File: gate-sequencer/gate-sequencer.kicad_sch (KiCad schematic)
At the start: 153 parts, among them J1 Gate 8, J10 Gate 6, J11 Gate 10, J12 Gate 14, J13 Gate 1, J14 Gate 5, J15 Gate 9, J16 Gate 13, J17 Clock, J18 Conn_01x34_Socket, J19 Power, J2 Gate 4, J20 Power, J21 Power, J22 Clock, J23 Gate 1, J24 Gate 9, J25 Gate 2, J26 Gate 10, J27 Gate 3, J28 Gate 11, J29 Gate 4, J3 Gate 12, J30 Gate 12, J31 Gate 5, J32 Gate 13, J33 Gate 6, J34 Gate 14, J35 Gate 7, J36 Gate 15, J37 Gate 8, J38 Gate 16, J39 LED, J4 Gate 16, J40 LED, J41 LED, J42 LED, J43 LED, J44 LED, J45 LED, J46 LED, J47 LED, J48 LED, J49 LED, J5 Gate 3, J50 LED, J51 LED, J52 LED, J53 LED, J54 LED, J55 Conn_01x34_Pin, J6 Gate 7, J7 Gate 11, J8 Gate 15, J9 Gate 2, SW1 X1, SW10 S6, SW11 S7, SW12 S8, SW13 S9, SW14 S10, SW15 S11, SW16 S12, SW17 S13, SW18 S14, SW19 S15, SW2 X2, SW20 S16, SW21 Mode, SW22 Mode 2, SW3 X3, SW35 Clock Source, SW4 X4, SW5 S1, SW6 S2, SW7 S3, SW8 S4, SW9 S5

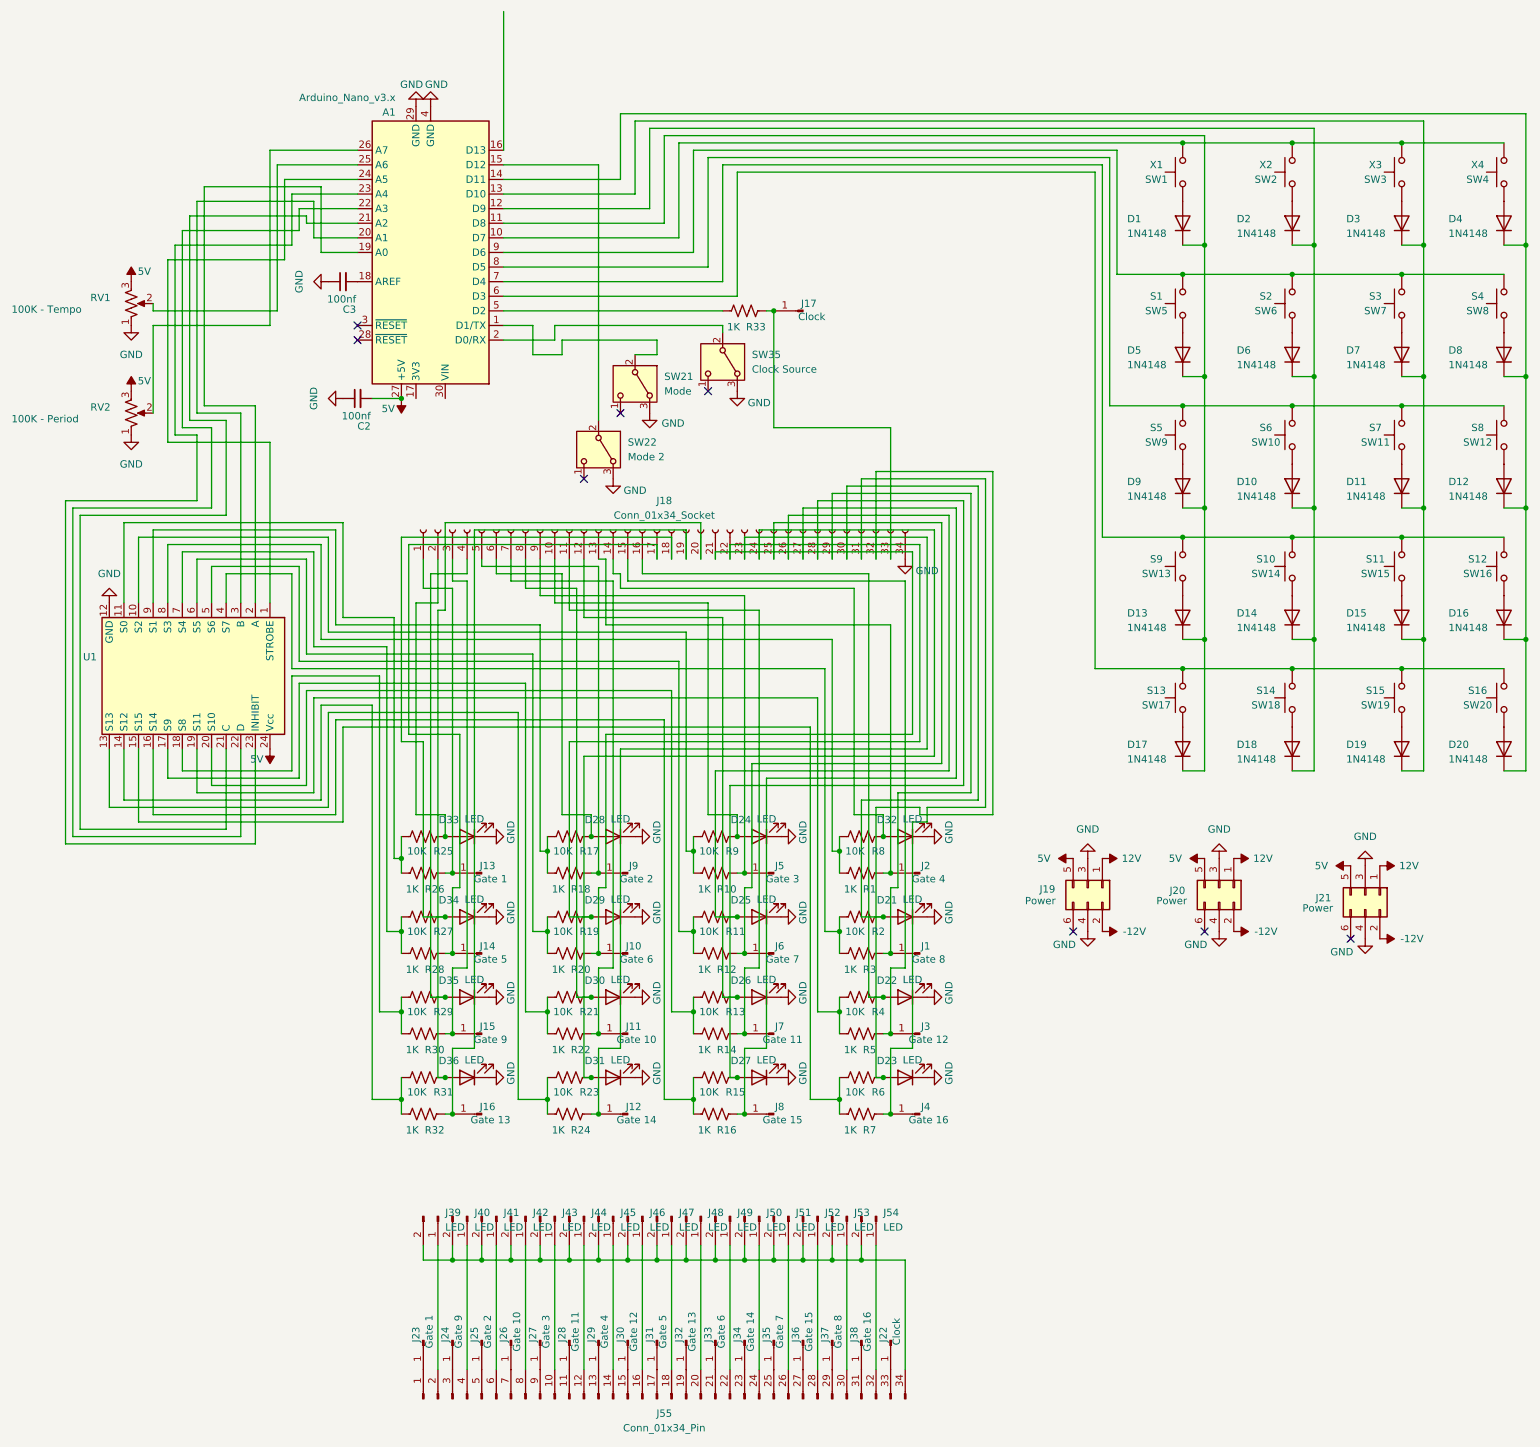
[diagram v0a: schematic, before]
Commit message: Renumber some components
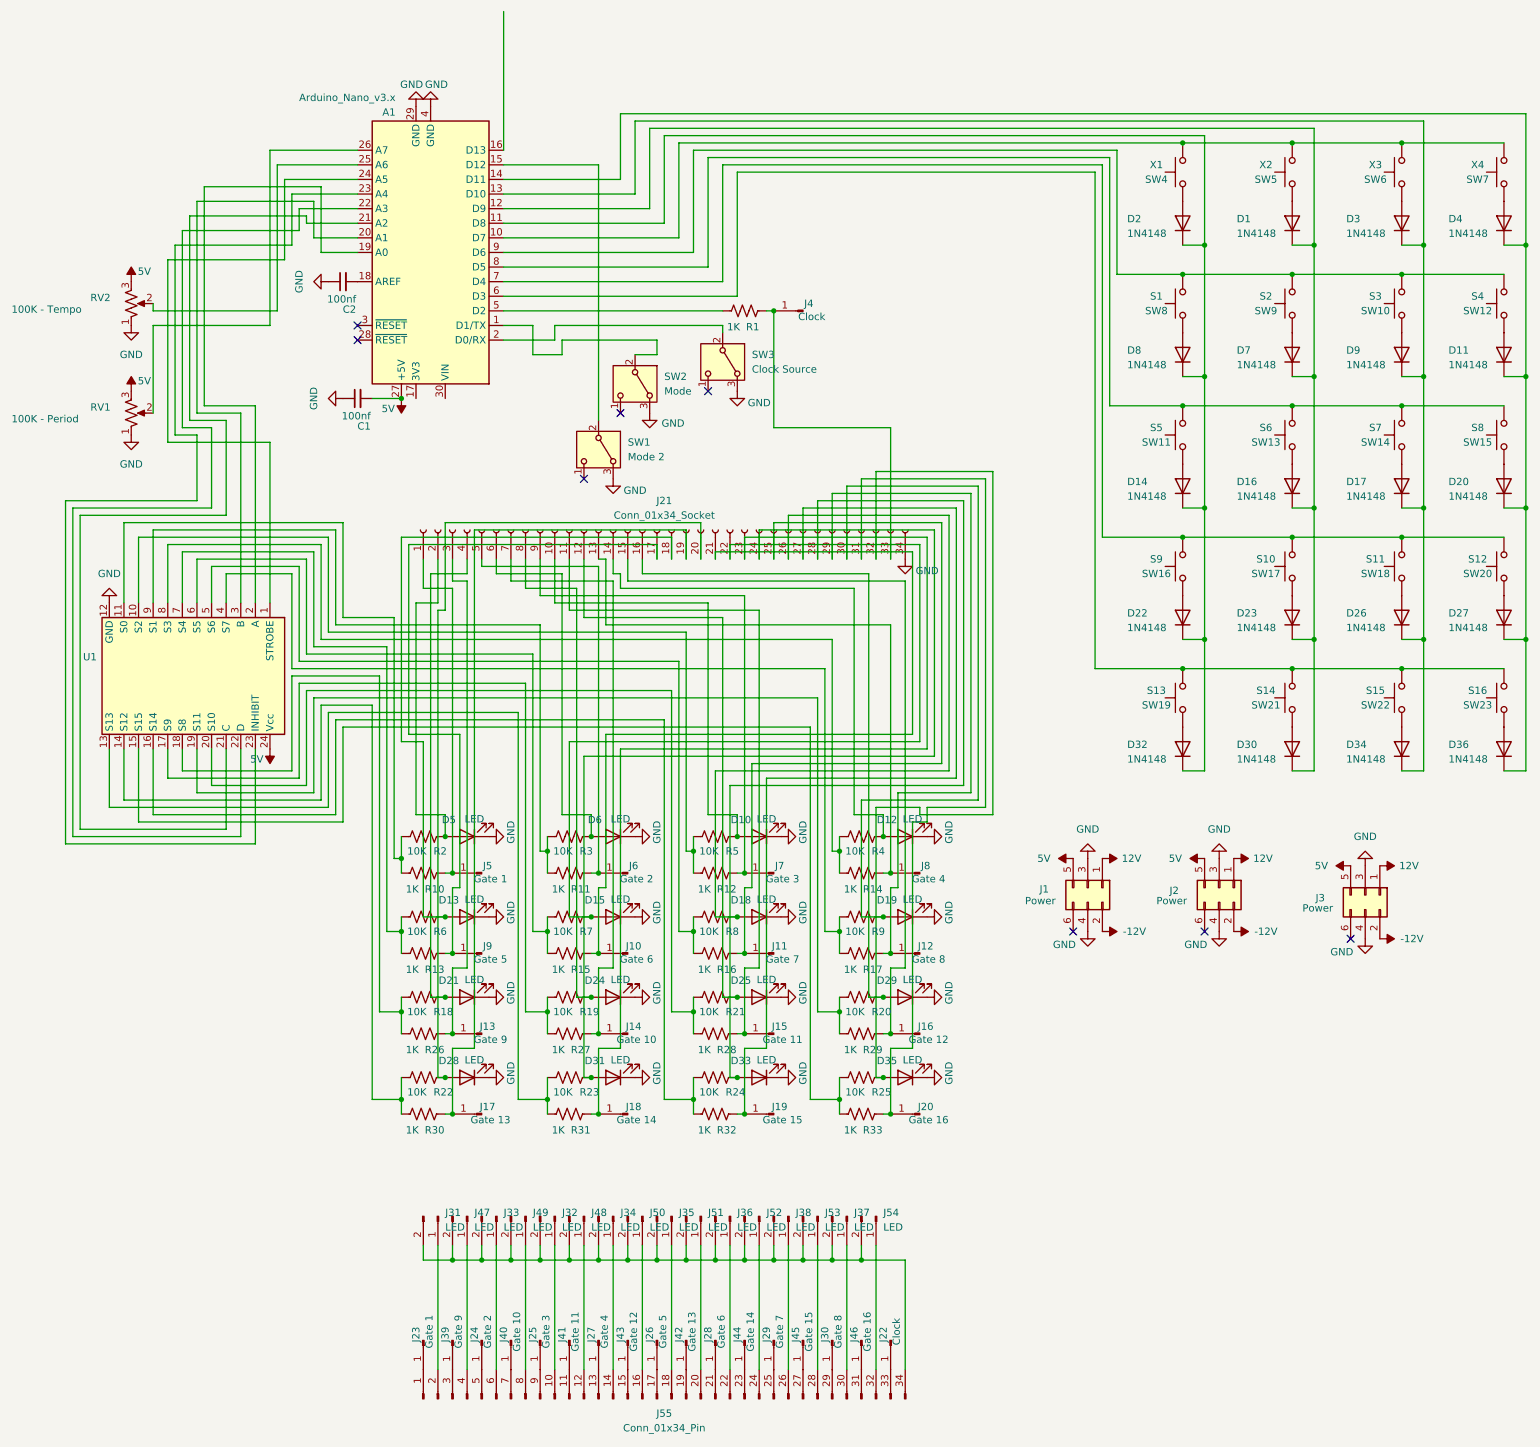
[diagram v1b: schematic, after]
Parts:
- renumbered C2 to C1, C3 to C2, D2 to D1, D24 to D10, D8 to D11, D32 to D12, D34 to D13, D9 to D14, D29 to D15, D10 to D16, D11 to D17, D25 to D18, D21 to D19, D1 to D2, D12 to D20, D35 to D21, D13 to D22, D14 to D23, D30 to D24, D26 to D25, D15 to D26, D16 to D27, D36 to D28, D22 to D29, D18 to D30, D17 to D32, D27 to D33, D19 to D34, D23 to D35, D20 to D36, D33 to D5, D28 to D6, D6 to D7, D5 to D8, D7 to D9, J19 to J1, J6 to J11, J1 to J12, J15 to J13, J11 to J14, J7 to J15, J3 to J16, J16 to J17, J12 to J18, J8 to J19, J20 to J2, J4 to J20, J18 to J21, J25 to J24, J27 to J25, J31 to J26, J29 to J27, J33 to J28, J35 to J29, J21 to J3, J37 to J30, J39 to J31, J43 to J32, J41 to J33, J45 to J34, J47 to J35, J49 to J36, J53 to J37, J51 to J38, J24 to J39, J17 to J4, J26 to J40, J28 to J41, J32 to J42, J30 to J43, J34 to J44, J36 to J45, J38 to J46, J40 to J47, J44 to J48, J42 to J49, J13 to J5, J46 to J50, J48 to J51, J50 to J52, J52 to J53, J9 to J6, J5 to J7, J2 to J8, J14 to J9, R33 to R1, R26 to R10, R18 to R11, R10 to R12, R28 to R13, R1 to R14, R20 to R15, R12 to R16, R3 to R17, R29 to R18, R21 to R19, R25 to R2, R4 to R20, R13 to R21, R31 to R22, R15 to R24, R6 to R25, R30 to R26, R22 to R27, R14 to R28, R5 to R29, R17 to R3, R32 to R30, R24 to R31, R16 to R32, R7 to R33, R8 to R4, R9 to R5, R27 to R6, R19 to R7, R11 to R8, R2 to R9, RV2 to RV1, RV1 to RV2, SW22 to SW1, SW7 to SW10, SW9 to SW11, SW8 to SW12, SW10 to SW13, SW11 to SW14, SW12 to SW15, SW13 to SW16, SW14 to SW17, SW15 to SW18, SW17 to SW19, SW21 to SW2, SW16 to SW20, SW18 to SW21, SW19 to SW22, SW20 to SW23, SW35 to SW3, SW1 to SW4, SW2 to SW5, SW3 to SW6, SW4 to SW7, SW5 to SW8, SW6 to SW9

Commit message: Revert "Renumber some components"
This reverts commit 4c9a93e4336de2276d9b49e02718b6a92f997a6a.
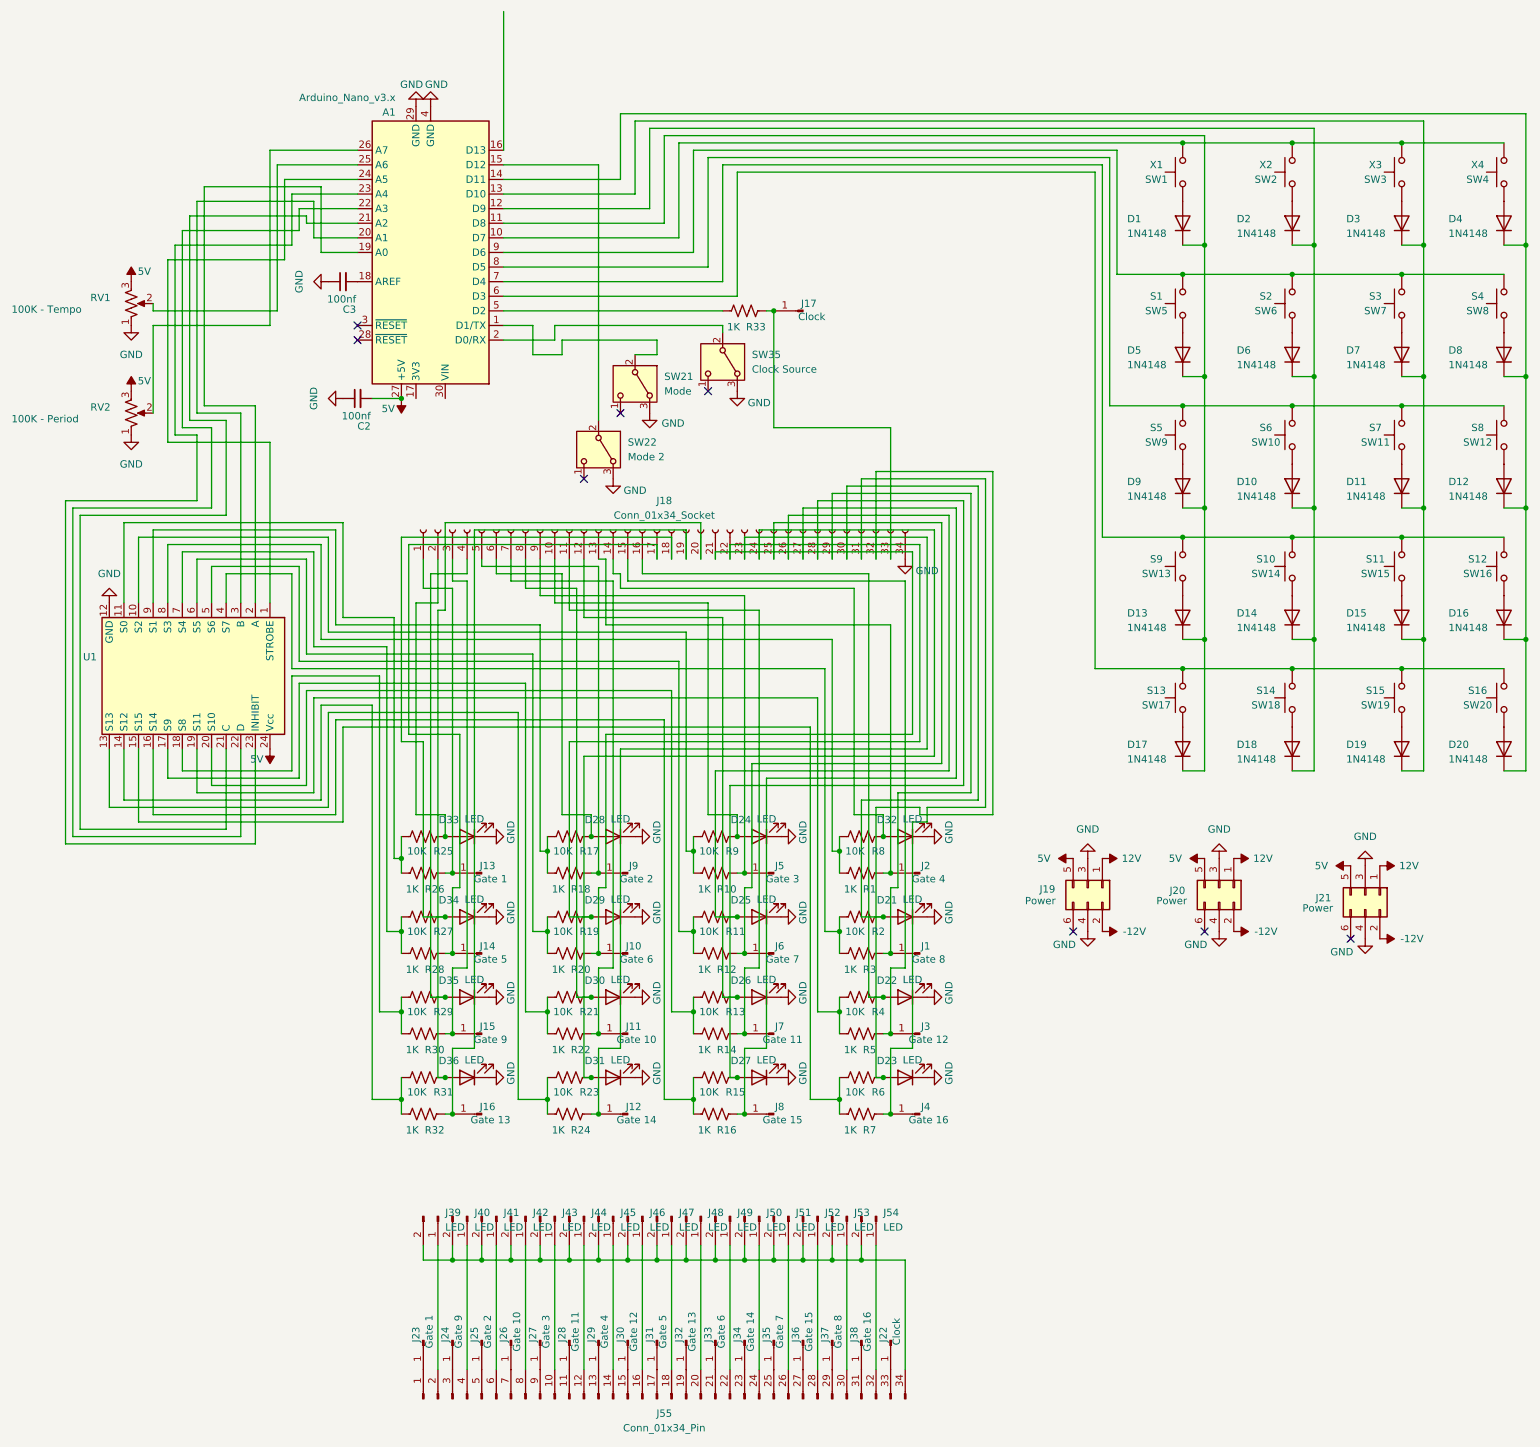
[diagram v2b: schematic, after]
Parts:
- renumbered C1 to C2, C2 to C3, D2 to D1, D16 to D10, D17 to D11, D20 to D12, D22 to D13, D23 to D14, D26 to D15, D27 to D16, D32 to D17, D30 to D18, D34 to D19, D1 to D2, D36 to D20, D19 to D21, D29 to D22, D35 to D23, D10 to D24, D18 to D25, D25 to D26, D33 to D27, D6 to D28, D15 to D29, D24 to D30, D12 to D32, D5 to D33, D13 to D34, D21 to D35, D28 to D36, D8 to D5, D7 to D6, D9 to D7, D11 to D8, D14 to D9, J12 to J1, J14 to J11, J18 to J12, J5 to J13, J9 to J14, J13 to J15, J17 to J16, J4 to J17, J21 to J18, J1 to J19, J8 to J2, J2 to J20, J3 to J21, J39 to J24, J24 to J25, J40 to J26, J25 to J27, J41 to J28, J27 to J29, J16 to J3, J43 to J30, J26 to J31, J42 to J32, J28 to J33, J44 to J34, J29 to J35, J45 to J36, J30 to J37, J46 to J38, J31 to J39, J20 to J4, J47 to J40, J33 to J41, J49 to J42, J32 to J43, J48 to J44, J34 to J45, J50 to J46, J35 to J47, J51 to J48, J36 to J49, J7 to J5, J52 to J50, J38 to J51, J53 to J52, J37 to J53, J11 to J6, J15 to J7, J19 to J8, J6 to J9, R14 to R1, R12 to R10, R8 to R11, R16 to R12, R21 to R13, R28 to R14, R24 to R15, R32 to R16, R3 to R17, R11 to R18, R7 to R19, R9 to R2, R15 to R20, R19 to R21, R27 to R22, R31 to R24, R2 to R25, R10 to R26, R6 to R27, R13 to R28, R18 to R29, R17 to R3, R26 to R30, R22 to R31, R30 to R32, R1 to R33, R20 to R4, R29 to R5, R25 to R6, R33 to R7, R4 to R8, R5 to R9, RV2 to RV1, RV1 to RV2, SW4 to SW1, SW13 to SW10, SW14 to SW11, SW15 to SW12, SW16 to SW13, SW17 to SW14, SW18 to SW15, SW20 to SW16, SW19 to SW17, SW21 to SW18, SW22 to SW19, SW5 to SW2, SW23 to SW20, SW2 to SW21, SW1 to SW22, SW6 to SW3, SW3 to SW35, SW7 to SW4, SW8 to SW5, SW9 to SW6, SW10 to SW7, SW12 to SW8, SW11 to SW9
